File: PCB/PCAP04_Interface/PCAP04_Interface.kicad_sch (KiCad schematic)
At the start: 39 parts, among them J1 Conn_01x04, J2 43045-2022, J3 MEM2067-02-180-00-A, J4 Conn_01x02, U1 PCAP_04-eva-board, U2 ESP-WROOM-32-DEVBOARD

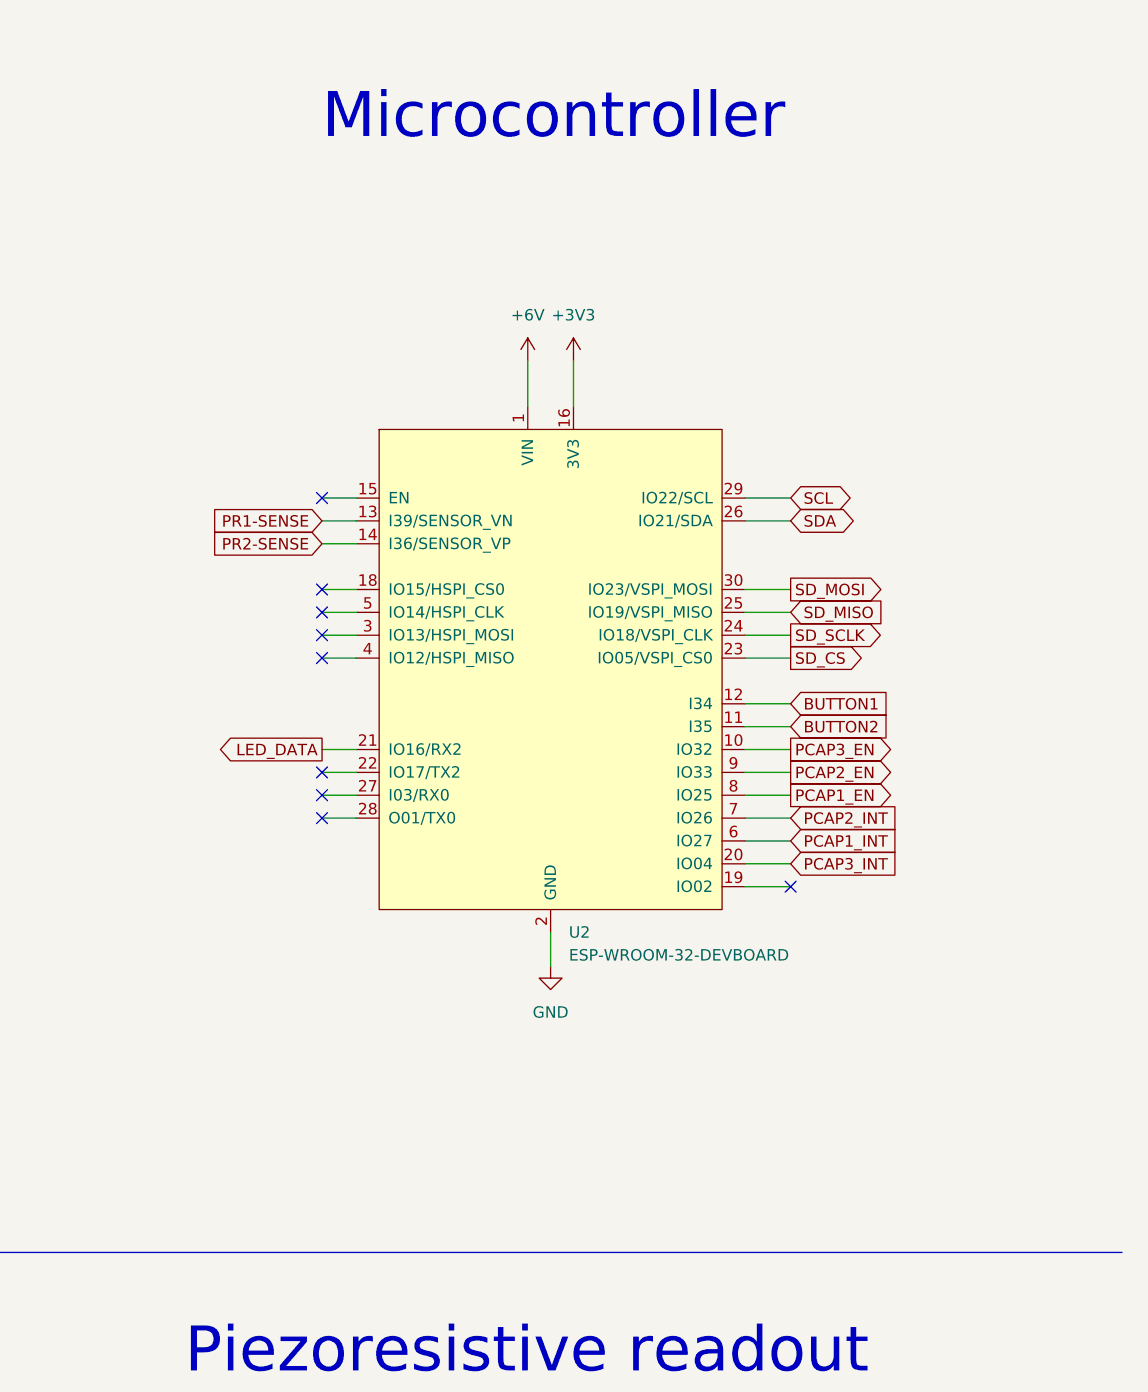
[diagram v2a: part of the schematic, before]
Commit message: Upgraded webserver functionalities
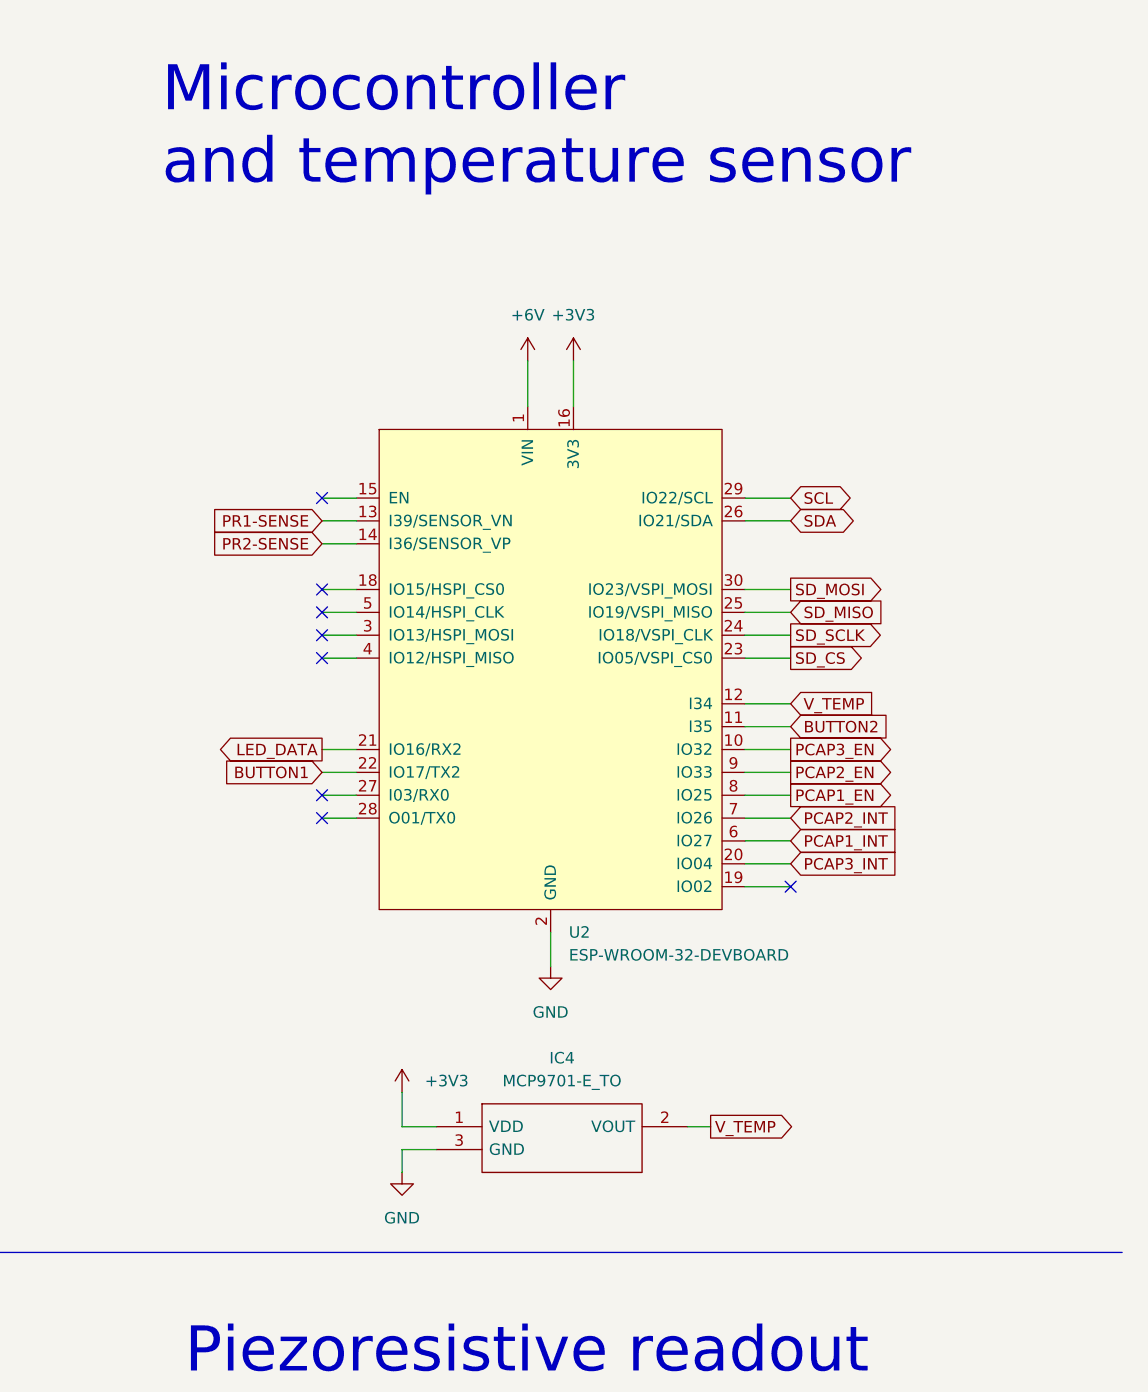
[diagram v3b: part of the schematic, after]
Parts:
- added IC4: MCP9701-E_TO, Package_TO_SOT_THT:TO-92_Inline, symbol SymbolLib:MCP9701-E_TO
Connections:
- net +3V3: now also IC4.1 (VDD)
- net BUTTON1: now also U2.22 (IO17/TX2); no longer U2.12 (I34)
- net GND: now also IC4.3 (GND)
- new net V_TEMP: IC4.2 (VOUT), U2.12 (I34)
- no-connect marks 27 -> 26
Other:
- note added: "Microcontroller and temperature sensor"
- note removed: "Microcontroller"
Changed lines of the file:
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@@
   (no_connect (at 318.77 77.47))
   (no_connect (at 318.77 80.01))
-  (no_connect (at 318.77 95.25))
   (no_connect (at 318.77 97.79))
   (no_connect (at 318.77 100.33))
@@
   (no_connect (at 207.01 260.35))
   (no_connect (at 204.47 260.35))
+  (wire (pts (xy 327.66 139.7) (xy 327.66 137.16))
+    (stroke (width 0) (type default) (color 0 0 0 0))
+  )
   (wire (pts (xy 313.69 187.96) (xy 313.69 198.12))
     (stroke (width 0) (type default) (color 0 0 0 0))
@@
     (stroke (width 0) (type default) (color 0 0 0 0))
   )
+  (wire (pts (xy 327.66 130.81) (xy 327.66 134.62))
+    (stroke (width 0) (type default) (color 0 0 0 0))
+  )
   (wire (pts (xy 232.41 57.15) (xy 237.49 57.15))
     (stroke (width 0) (type default) (color 0 0 0 0))
@@
     (stroke (width 0) (type default) (color 0 0 0 0))
   )
+  (wire (pts (xy 359.41 134.62) (xy 361.95 134.62))
+    (stroke (width 0) (type default) (color 0 0 0 0))
+  )
   (wire (pts (xy 233.68 196.85) (xy 233.68 199.39))
     (stroke (width 0) (type default) (color 0 0 0 0))
@@
     (stroke (width 0) (type default) (color 0 0 0 0))
   )
+  (wire (pts (xy 327.66 137.16) (xy 331.47 137.16))
+    (stroke (width 0) (type default) (color 0 0 0 0))
+  )
   (wire (pts (xy 82.55 127) (xy 82.55 129.54))
     (stroke (width 0) (type default) (color 0 0 0 0))
@@
     (stroke (width 0) (type default) (color 0 0 0 0))
   )
+  (wire (pts (xy 365.76 87.63) (xy 370.84 87.63))
+    (stroke (width 0) (type default) (color 0 0 0 0))
+  )
   (wire (pts (xy 318.77 74.93) (xy 322.58 74.93))
     (stroke (width 0) (type default) (color 0 0 0 0))
@@
     (stroke (width 0) (type default) (color 0 0 0 0))
   )
+  (wire (pts (xy 327.66 134.62) (xy 331.47 134.62))
+    (stroke (width 0) (type default) (color 0 0 0 0))
+  )
   (polyline (pts (xy 276.86 12.7) (xy 276.86 285.75))
     (stroke (width 0) (type default) (color 0 0 0 0))
@@
     (stroke (width 0) (type default) (color 0 0 0 0))
   )
-  (wire (pts (xy 365.76 87.63) (xy 370.84 87.63))
-    (stroke (width 0) (type default) (color 0 0 0 0))
-  )
   (wire (pts (xy 233.68 191.77) (xy 233.68 194.31))
     (stroke (width 0) (type default) (color 0 0 0 0))
@@
     (effects (font (size 1.27 1.27)) (justify left bottom))
   )
-  (text "Microcontroller" (at 318.77 25.4 0)
+  (text "Microcontroller\nand temperature sensor" (at 300.99 30.48 0)
     (effects (font (size 5 5)) (justify left bottom))
   )
@@
     )
   )
+  (global_label "V_TEMP" (shape output) (at 361.95 134.62 0) (fields_autoplaced)
+    (effects (font (size 1.27 1.27)) (justify left))
+    (property "Intersheet References" "${INTERSHEET_REFS}" (id 0) (at 371.2574 134.5406 0)
+      (effects (font (size 1.27 1.27)) (justify left) hide)
+    )
+  )
   (global_label "C1.5" (shape input) (at 196.85 177.8 180) (fields_autoplaced)
     (effects (font (size 1.27 1.27)) (justify right))
@@
     )
   )
-  (global_label "BUTTON1" (shape input) (at 370.84 87.63 0) (fields_autoplaced)
-    (effects (font (size 1.27 1.27)) (justify left))
-    (property "Intersheet References" "${INTERSHEET_REFS}" (id 0) (at 381.6593 87.7094 0)
-      (effects (font (size 1.27 1.27)) (justify left) hide)
+  (global_label "BUTTON1" (shape input) (at 318.77 95.25 180) (fields_autoplaced)
+    (effects (font (size 1.27 1.27)) (justify right))
+    (property "Intersheet References" "${INTERSHEET_REFS}" (id 0) (at 307.9507 95.1706 0)
+      (effects (font (size 1.27 1.27)) (justify right) hide)
     )
   )
@@
     )
   )
+  (global_label "V_TEMP" (shape input) (at 370.84 87.63 0) (fields_autoplaced)
+    (effects (font (size 1.27 1.27)) (justify left))
+    (property "Intersheet References" "${INTERSHEET_REFS}" (id 0) (at 380.1474 87.5506 0)
+      (effects (font (size 1.27 1.27)) (justify left) hide)
+    )
+  )
   (global_label "LED_DATA" (shape input) (at 185.42 116.84 180) (fields_autoplaced)
     (effects (font (size 1.27 1.27)) (justify right))
@@
     (pin "1")
   )
+  (symbol (lib_id "power:+3V3") (at 327.66 130.81 0) (unit 1)
+    (in_bom yes) (on_board yes) (fields_autoplaced)
+    (property "Reference" "#PWR0103" (id 0) (at 327.66 134.62 0)
+      (effects (font (size 1.27 1.27)) hide)
+    )
+    (property "Value" "+3V3" (id 1) (at 330.2 129.5399 0)
+      (effects (font (size 1.27 1.27)) (justify left))
+    )
+    (property "Footprint" "" (id 2) (at 327.66 130.81 0)
+      (effects (font (size 1.27 1.27)) hide)
+    )
+    (property "Datasheet" "" (id 3) (at 327.66 130.81 0)
+      (effects (font (size 1.27 1.27)) hide)
+    )
+    (pin "1")
+  )
   (symbol (lib_id "power:GND") (at 95.25 198.12 0) (unit 1)
     (in_bom yes) (on_board yes)
@@
     (pin "2")
   )
+  (symbol (lib_id "power:GND") (at 327.66 139.7 0) (unit 1)
+    (in_bom yes) (on_board yes) (fields_autoplaced)
+    (property "Reference" "#PWR0104" (id 0) (at 327.66 146.05 0)
+      (effects (font (size 1.27 1.27)) hide)
+    )
+    (property "Value" "GND" (id 1) (at 327.66 144.78 0))
+    (property "Footprint" "" (id 2) (at 327.66 139.7 0)
+      (effects (font (size 1.27 1.27)) hide)
+    )
+    (property "Datasheet" "" (id 3) (at 327.66 139.7 0)
+      (effects (font (size 1.27 1.27)) hide)
+    )
+    (pin "1")
+  )
   (symbol (lib_id "Device:C") (at 259.08 199.39 270) (unit 1)
     (in_bom yes) (on_board yes) (fields_autoplaced)
@@
     (pin "2")
   )
+  (symbol (lib_id "SymbolLib:MCP9701-E_TO") (at 331.47 134.62 0) (unit 1)
+    (in_bom yes) (on_board yes) (fields_autoplaced)
+    (property "Reference" "IC4" (id 0) (at 345.44 127 0))
+    (property "Value" "MCP9701-E_TO" (id 1) (at 345.44 129.54 0))
+    (property "Footprint" "Package_TO_SOT_THT:TO-92_Inline" (id 2) (at 355.6 132.08 0)
+      (effects (font (size 1.27 1.27)) (justify left) hide)
+    )
+    (property "Datasheet" "http://componentsearchengine.com/Datasheets/3/MCP9701-E_TO.pdf" (id 3) (at 355.6 134.62 0)
+      (effects (font (size 1.27 1.27)) (justify left) hide)
+    )
+    (property "Description" "Microchip MCP9701-E/TO Temperature Sensor 3-Pin TO-92, -10  +125 C" (id 4) (at 355.6 137.16 0)
+      (effects (font (size 1.27 1.27)) (justify left) hide)
+    )
+    (property "Mouser Part Number" "579-MCP9701-E/TO" (id 5) (at 355.6 142.24 0)
+      (effects (font (size 1.27 1.27)) (justify left) hide)
+    )
+    (property "Mouser Price/Stock" "https://www.mouser.co.uk/ProductDetail/Microchip-Technology/MCP9701-E-TO?qs=RnzODY3cU8tNZFvtanRw3w%3D%3D" (id 6) (at 355.6 144.78 0)
+      (effects (font (size 1.27 1.27)) (justify left) hide)
+    )
+    (property "Manufacturer_Name" "Microchip" (id 7) (at 355.6 147.32 0)
+      (effects (font (size 1.27 1.27)) (justify left) hide)
+    )
+    (property "Manufacturer_Part_Number" "MCP9701-E/TO" (id 8) (at 355.6 149.86 0)
+      (effects (font (size 1.27 1.27)) (justify left) hide)
+    )
+    (pin "1")
+    (pin "2")
+    (pin "3")
+  )
   (symbol (lib_id "Device:C") (at 186.69 191.77 270) (unit 1)
     (in_bom yes) (on_board yes) (fields_autoplaced)
@@
       (reference "#PWR0102") (unit 1) (value "+6V") (footprint "")
     )
+    (path "/5e95227e-f3b3-4cf5-98d6-f51bee14984f"
+      (reference "#PWR0103") (unit 1) (value "+3V3") (footprint "")
+    )
+    (path "/6d0ca0a0-f8c6-4db7-bde6-2df79487706d"
+      (reference "#PWR0104") (unit 1) (value "GND") (footprint "")
+    )
     (path "/5138298e-c4e5-4c8d-ac1b-c9637b29d4c5"
       (reference "C1") (unit 1) (value "2p") (footprint "Capacitor_SMD:C_0603_1608Metric_Pad1.08x0.95mm_HandSolder")
@@
       (reference "IC3") (unit 1) (value "PCAP04-AQFM-24") (footprint "FootrpintLib:PCAP04AQFM24")
     )
+    (path "/c54d1fa1-ebc0-44f5-917e-3306417c744f"
+      (reference "IC4") (unit 1) (value "MCP9701-E_TO") (footprint "Package_TO_SOT_THT:TO-92_Inline")
+    )
     (path "/e6367e4e-fbdb-4e0e-bb4a-deae4997ff2f"

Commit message: Poging tot config
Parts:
- added C30: 22u, Capacitor_Tantalum_SMD:CP_EIA-1608-10_AVX-L_Pad1.25x1.05mm_HandSolder, symbol Device:C_Polarized
- added J5: Conn_02x06_Odd_Even, Connector_PinHeader_2.54mm:PinHeader_2x06_P2.54mm_Vertical, symbol Connector_Generic:Conn_02x06_Odd_Even
- added J6: Conn_02x03_Odd_Even, Connector_PinHeader_2.54mm:PinHeader_2x03_P2.54mm_Vertical, symbol Connector_Generic:Conn_02x03_Odd_Even
- added U3: AMS1117-3.3, Package_TO_SOT_SMD:SOT-223-3_TabPin2, symbol Regulator_Linear:AMS1117-3.3
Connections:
- net +3V3: now also C30.1, J5.2 (Pin_2), U3.2 (VO); no longer U2.16 (3V3)
- net +6V: now also J5.3 (Pin_3)
- net +BATT: now also U3.3 (VI)
- net BUTTON1: now also U2.21 (IO16/RX2); no longer U2.22 (IO17/TX2)
- net BUTTON2: now also U2.22 (IO17/TX2); no longer U2.11 (I35)
- net GND: now also C30.2, J5.1 (Pin_1), J5.11 (Pin_11), J6.6 (Pin_6), U3.1 (GND); no longer J1.1 (Pin_1)
- net LED_DATA: now also U2.8 (IO25); no longer U2.21 (IO16/RX2)
- net PCAP1_EN: now also U2.3 (IO13/HSPI_MOSI); no longer U2.8 (IO25)
- net PCAP2_EN: now also U2.5 (IO14/HSPI_CLK); no longer U2.9 (IO33)
- net PCAP3_EN: now also U2.18 (IO15/HSPI_CS0); no longer U2.10 (IO32)
- net SCL: now also J5.12 (Pin_12)
- net SDA: now also J5.10 (Pin_10)
- net SD_MISO: now also J5.8 (Pin_8)
- net SD_MOSI: now also J5.7 (Pin_7)
- net SD_SCLK: now also J5.9 (Pin_9)
- net B+: now reaches J1.4 (Pin_4)
- net B+: now also J6.1 (Pin_1); no longer D1.2
- net BM: now reaches J1.2 (Pin_2), J1.3 (Pin_3)
- net BM: now also J6.3 (Pin_3)
- new net B-: J1.1 (Pin_1), J6.5 (Pin_5)
- new net I35: J5.6 (Pin_6), U2.11 (I35)
- new net IO32: J5.5 (Pin_5), U2.10 (IO32)
- new net IO33: J5.4 (Pin_4), U2.9 (IO33)
- new net P+: D1.2, J6.2 (Pin_2)
- no-connect marks 26 -> 24
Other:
- note added: "Breakout for optional extra features"
- note added: "Breakout for unused ports"
- note added: "Offset capacitors"
- moved on the sheet: C15, C16, C17, C18, C19, C20, C21, C22, C23, C24, C25, C26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
